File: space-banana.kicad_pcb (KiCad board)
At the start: 2 copper layers, 229.6 x 135.2 mm, 119 parts, among them J1 ICSP, SW1 SW_PUSH, U1 ATMEGA32U4-MU, X1 ABM3-16.000

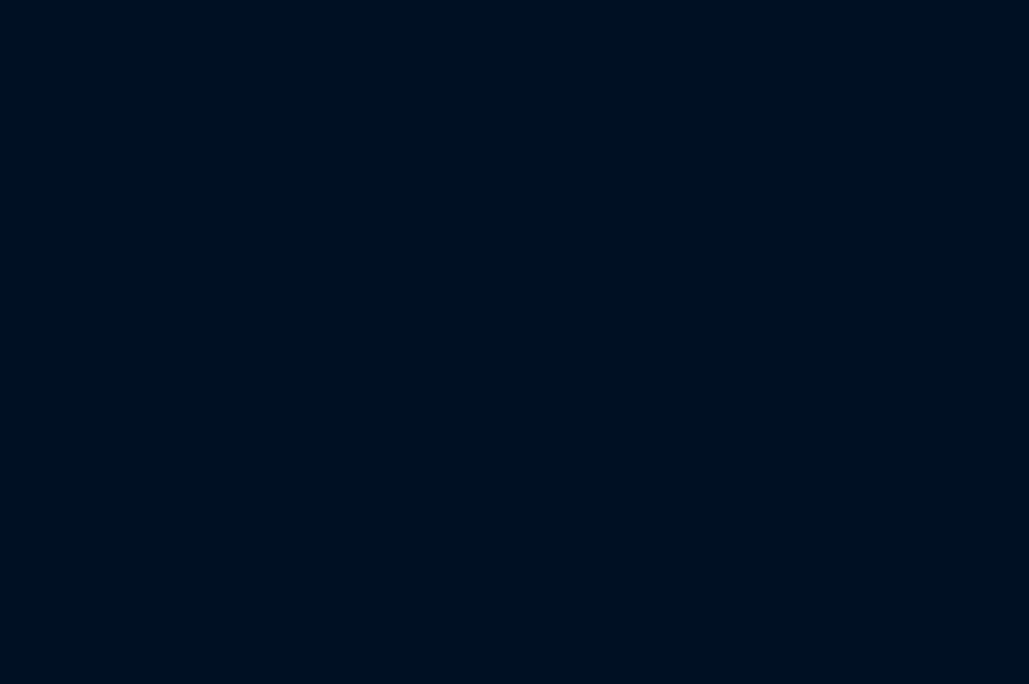
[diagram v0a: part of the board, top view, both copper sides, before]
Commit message: sync schematic to pcb
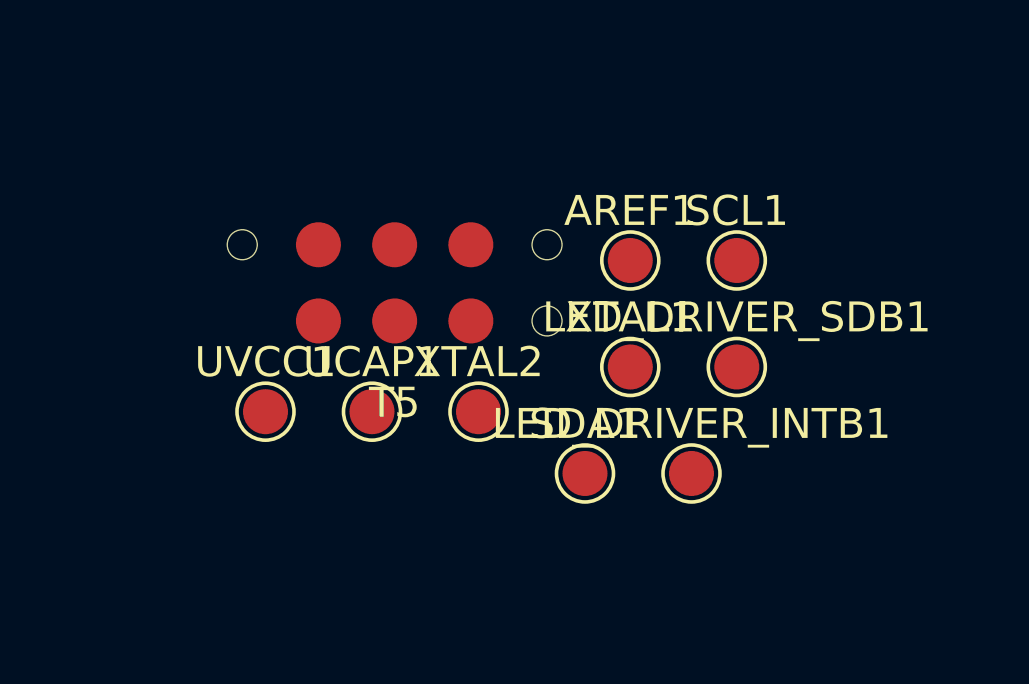
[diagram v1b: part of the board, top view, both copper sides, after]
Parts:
- added AREF1: TST, TestPoint:TestPoint_Pad_D1.5mm, F.Cu at (269.8, 40.4)
- added LED_DRIVER_INTB1: TST, TestPoint:TestPoint_Pad_D1.5mm, F.Cu at (271.8, 47.5)
- added LED_DRIVER_SDB1: TST, TestPoint:TestPoint_Pad_D1.5mm, F.Cu at (273.3, 44.0)
- added SCL1: TST, TestPoint:TestPoint_Pad_D1.5mm, F.Cu at (273.3, 40.4)
- added SDA1: TST, TestPoint:TestPoint_Pad_D1.5mm, F.Cu at (268.3, 47.5)
- added T5: ICSP_Test, Keyboardio:Six_Pin_Test_Point, F.Cu at (261.9, 41.2)
- added UCAP1: TST, TestPoint:TestPoint_Pad_D1.5mm, F.Cu at (261.2, 45.5)
- added UVCC1: TST, TestPoint:TestPoint_Pad_D1.5mm, F.Cu at (257.6, 45.5)
- added XTAL1: TST, TestPoint:TestPoint_Pad_D1.5mm, F.Cu at (269.8, 44.0)
- added XTAL2: TST, TestPoint:TestPoint_Pad_D1.5mm, F.Cu at (264.7, 45.5)
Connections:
- D2 pad 1: (no net) -> +5V
- D2 pad 2: (no net) -> /MCU-ATmega32u4/RESET_MCU
